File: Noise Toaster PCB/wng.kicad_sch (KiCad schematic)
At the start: 12 parts, among them Q2 2N3904, Q5 2N3904, Q6 2N3904

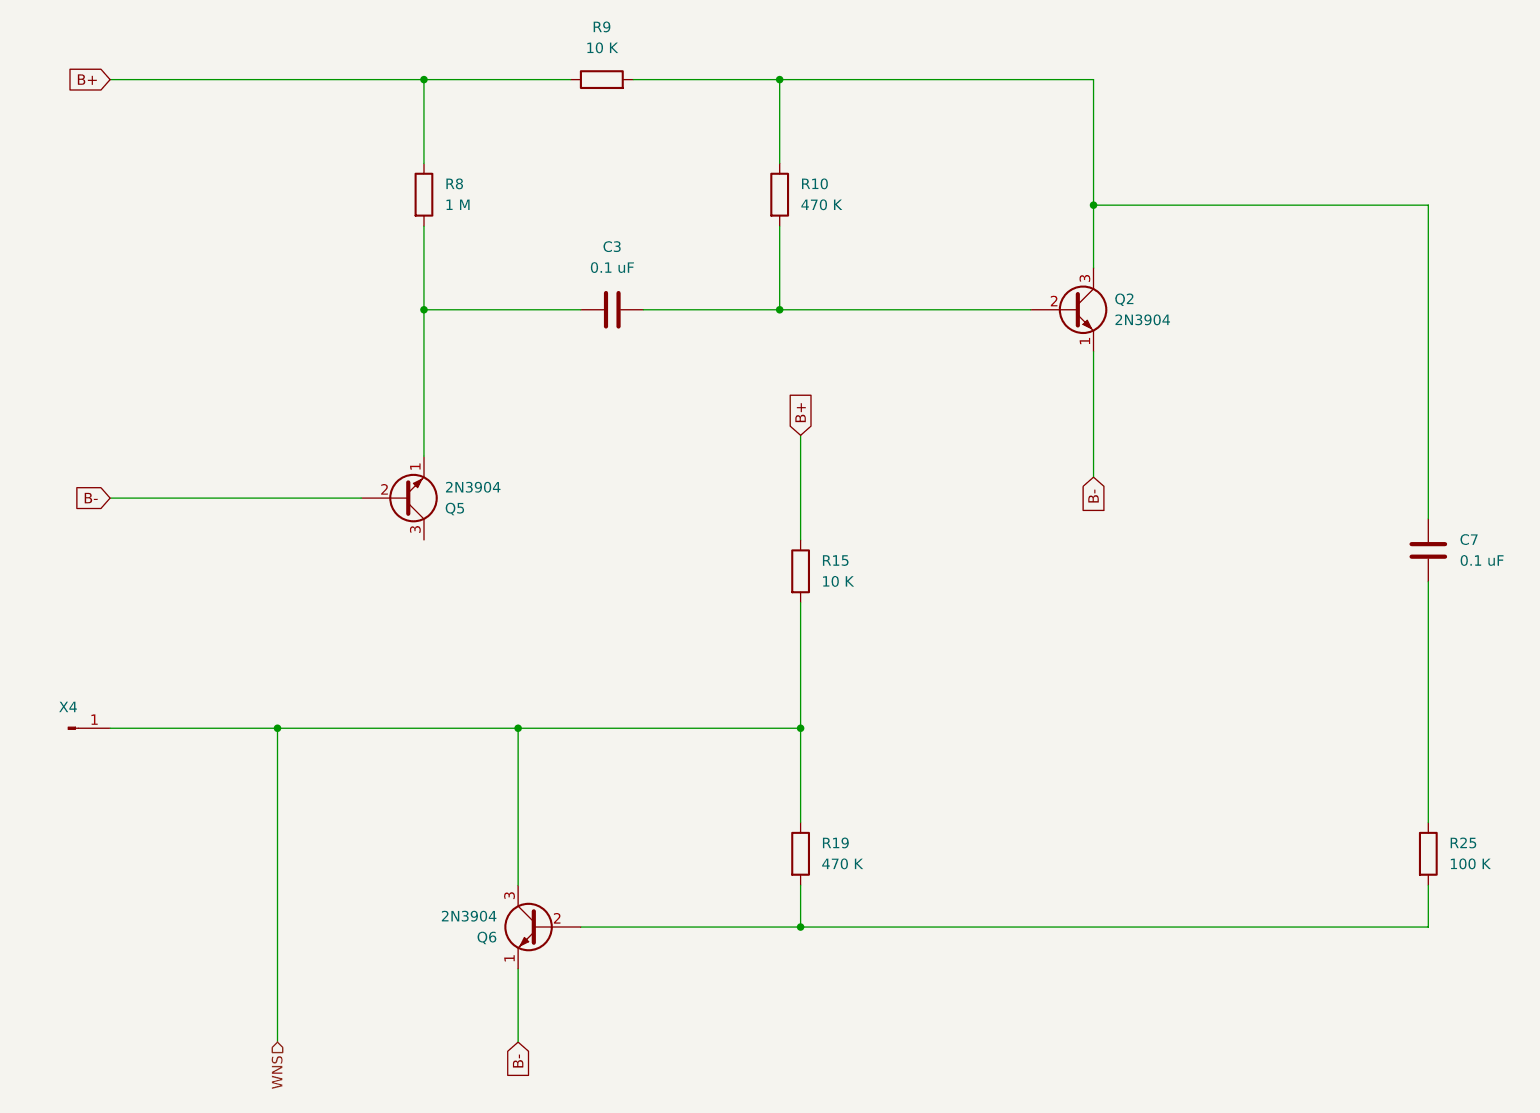
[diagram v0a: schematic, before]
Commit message: updated schematics
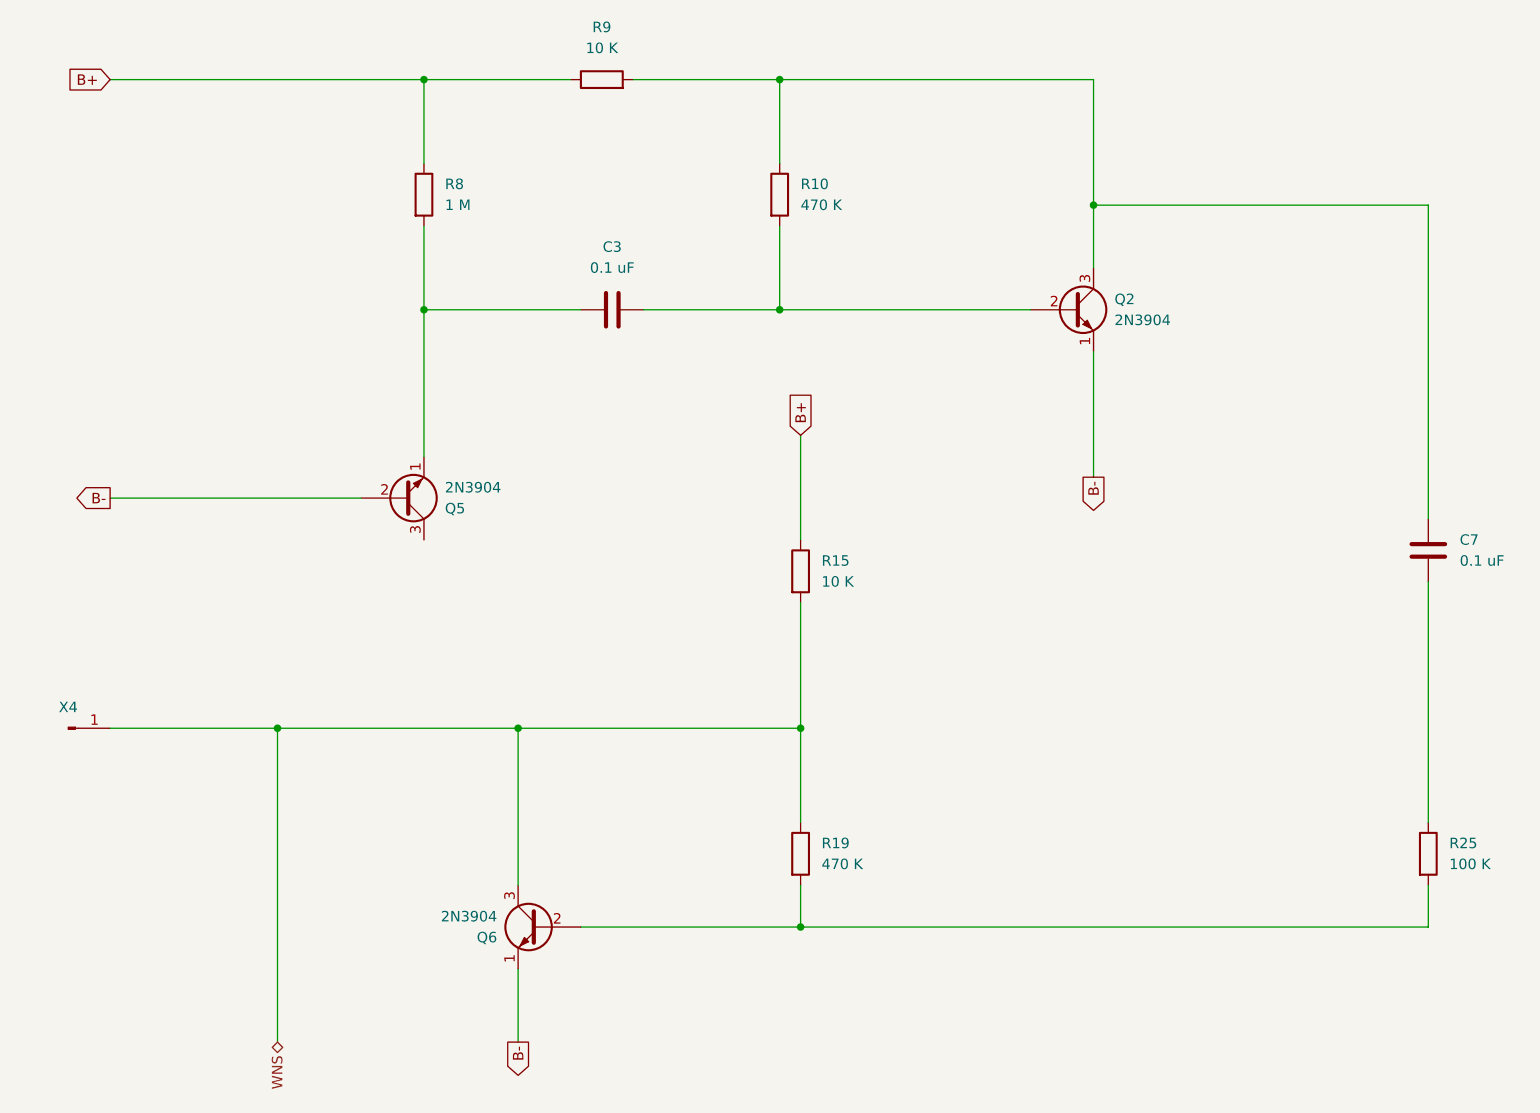
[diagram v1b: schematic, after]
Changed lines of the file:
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@@
     (stroke (width 0) (type default))
   )
-  (global_label "B-" (shape input) (at 118.11 165.1 270) (fields_autoplaced)
+  (global_label "B-" (shape output) (at 118.11 165.1 270) (fields_autoplaced)
     (effects (font (size 1.27 1.27)) (justify right))
     (property "Intersheetrefs" "${INTERSHEET_REFS}" (at 118.11 170.9276 90)
@@
     )
   )
-  (global_label "B-" (shape input) (at 187.96 96.52 270) (fields_autoplaced)
+  (global_label "B-" (shape output) (at 187.96 96.52 270) (fields_autoplaced)
     (effects (font (size 1.27 1.27)) (justify right))
     (property "Intersheetrefs" "${INTERSHEET_REFS}" (at 187.96 102.3476 90)
@@
     )
   )
-  (global_label "B-" (shape input) (at 68.58 99.06 180) (fields_autoplaced)
+  (global_label "B-" (shape output) (at 68.58 99.06 180) (fields_autoplaced)
     (effects (font (size 1.27 1.27)) (justify right))
     (property "Intersheetrefs" "${INTERSHEET_REFS}" (at 62.7524 99.06 0)
@@
     )
   )
-  (hierarchical_label "WNS" (shape input) (at 88.9 165.1 270) (fields_autoplaced)
+  (hierarchical_label "WNS" (shape bidirectional) (at 88.9 165.1 270) (fields_autoplaced)
     (effects (font (size 1.27 1.27)) (justify right))
   )

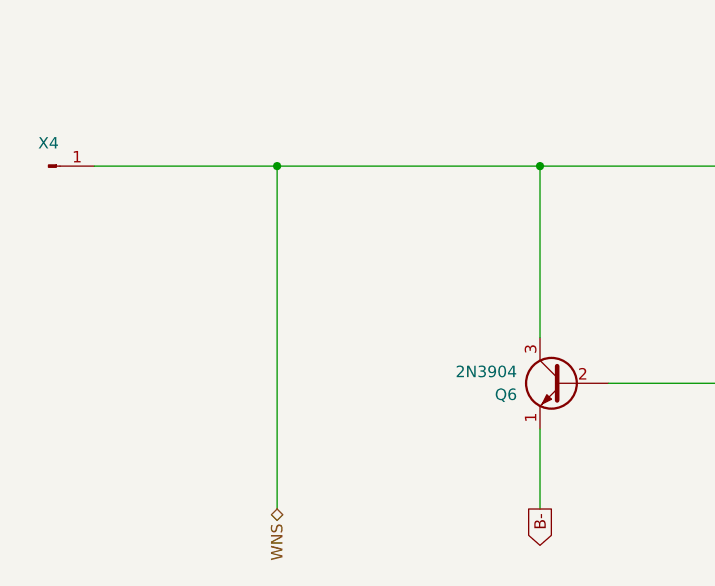
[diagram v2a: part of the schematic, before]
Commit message: refactored schematics and added front panel
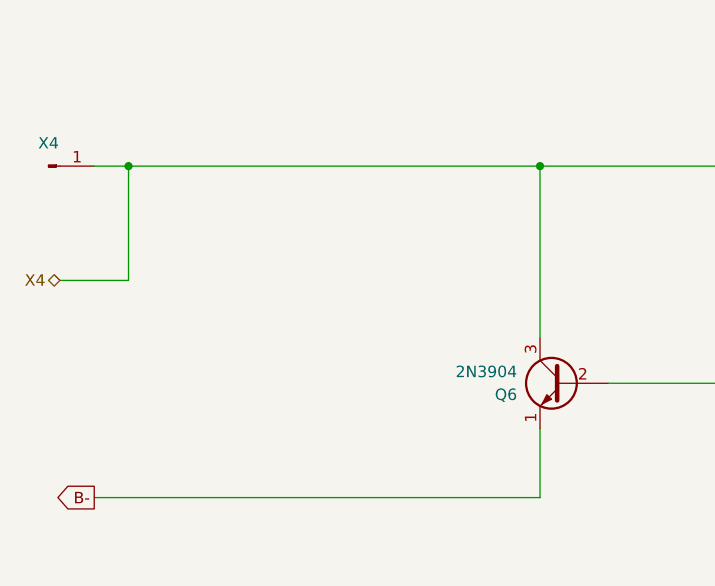
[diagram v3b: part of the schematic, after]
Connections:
- net WNS renamed X4
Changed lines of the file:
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@@
   (junction (at 106.68 48.26) (diameter 0) (color 0 0 0 0)
+  )
+  (junction (at 72.39 127) (diameter 0) (color 0 0 0 0)
   )
   (junction (at 187.96 63.5) (diameter 0) (color 0 0 0 0)
@@
   )
   (junction (at 149.86 76.2) (diameter 0) (color 0 0 0 0)
-  )
-  (junction (at 88.9 127) (diameter 0) (color 0 0 0 0)
   )
   (junction (at 106.68 76.2) (diameter 0) (color 0 0 0 0)
@@
     (stroke (width 0) (type default))
   )
-  (wire (pts (xy 118.11 156.21) (xy 118.11 165.1))
-    (stroke (width 0) (type default))
-  )
   (wire (pts (xy 149.86 76.2) (xy 180.34 76.2))
     (stroke (width 0) (type default))
   )
   (wire (pts (xy 106.68 76.2) (xy 125.73 76.2))
-    (stroke (width 0) (type default))
-  )
-  (wire (pts (xy 88.9 127) (xy 88.9 165.1))
     (stroke (width 0) (type default))
   )
@@
     (stroke (width 0) (type default))
   )
+  (wire (pts (xy 64.77 139.7) (xy 72.39 139.7))
+    (stroke (width 0) (type default))
+  )
   (wire (pts (xy 125.73 151.13) (xy 152.4 151.13))
     (stroke (width 0) (type default))
@@
     (stroke (width 0) (type default))
   )
+  (wire (pts (xy 118.11 163.83) (xy 118.11 156.21))
+    (stroke (width 0) (type default))
+  )
+  (wire (pts (xy 68.58 127) (xy 72.39 127))
+    (stroke (width 0) (type default))
+  )
+  (wire (pts (xy 72.39 127) (xy 118.11 127))
+    (stroke (width 0) (type default))
+  )
   (wire (pts (xy 152.4 91.44) (xy 152.4 104.14))
     (stroke (width 0) (type default))
   )
   (wire (pts (xy 133.35 76.2) (xy 149.86 76.2))
-    (stroke (width 0) (type default))
-  )
-  (wire (pts (xy 68.58 127) (xy 88.9 127))
     (stroke (width 0) (type default))
   )
@@
     (stroke (width 0) (type default))
   )
+  (wire (pts (xy 68.58 163.83) (xy 118.11 163.83))
+    (stroke (width 0) (type default))
+  )
   (wire (pts (xy 187.96 63.5) (xy 187.96 48.26))
     (stroke (width 0) (type default))
   )
-  (wire (pts (xy 187.96 81.28) (xy 187.96 96.52))
+  (wire (pts (xy 72.39 139.7) (xy 72.39 127))
     (stroke (width 0) (type default))
   )
-  (wire (pts (xy 88.9 127) (xy 118.11 127))
+  (wire (pts (xy 187.96 81.28) (xy 187.96 96.52))
     (stroke (width 0) (type default))
   )
@@
     (stroke (width 0) (type default))
   )
-  (global_label "B-" (shape output) (at 118.11 165.1 270) (fields_autoplaced)
+  (global_label "B-" (shape output) (at 68.58 163.83 180) (fields_autoplaced)
     (effects (font (size 1.27 1.27)) (justify right))
-    (property "Intersheetrefs" "${INTERSHEET_REFS}" (at 118.11 170.9276 90)
+    (property "Intersheetrefs" "${INTERSHEET_REFS}" (at 62.7524 163.83 0)
       (effects (font (size 1.27 1.27)) (justify right) hide)
     )
@@
     )
   )
-  (hierarchical_label "WNS" (shape bidirectional) (at 88.9 165.1 270)
+  (hierarchical_label "X4" (shape bidirectional) (at 64.77 139.7 180)
     (effects (font (size 1.27 1.27)) (justify right))
-    (property "Bezeichnung" "X4" (at 86.36 165.1 0)
-      (effects (font (size 1.27 1.27) italic) (justify right))
+    (property "Bezeichnung" "WNS" (at 60.96 137.16 0)
+      (effects (font (size 1.27 1.27) italic) (justify left))
     )
   )

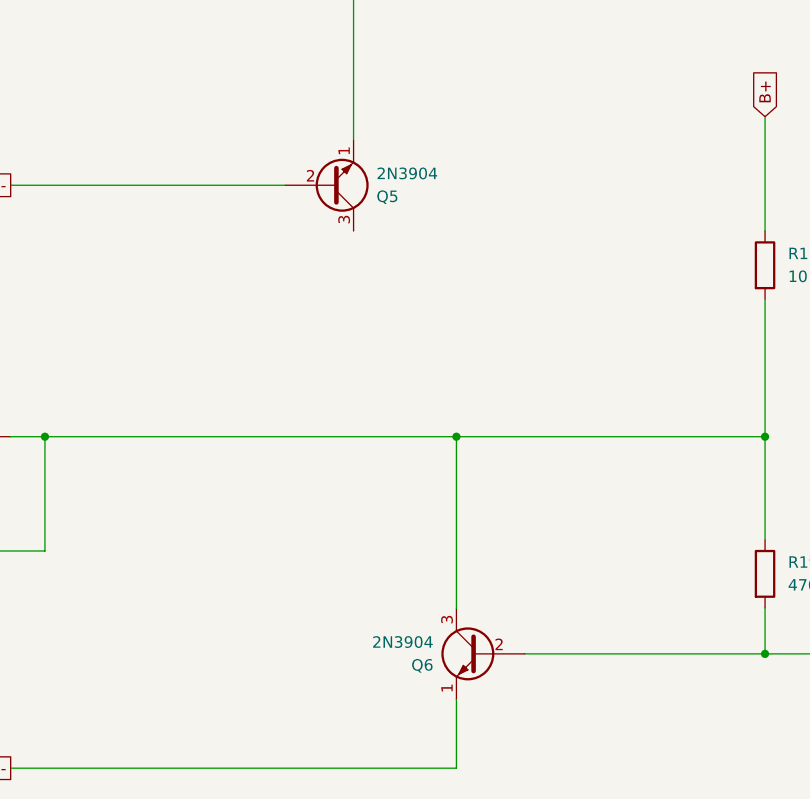
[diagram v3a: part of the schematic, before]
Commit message: wireing and components have been checked
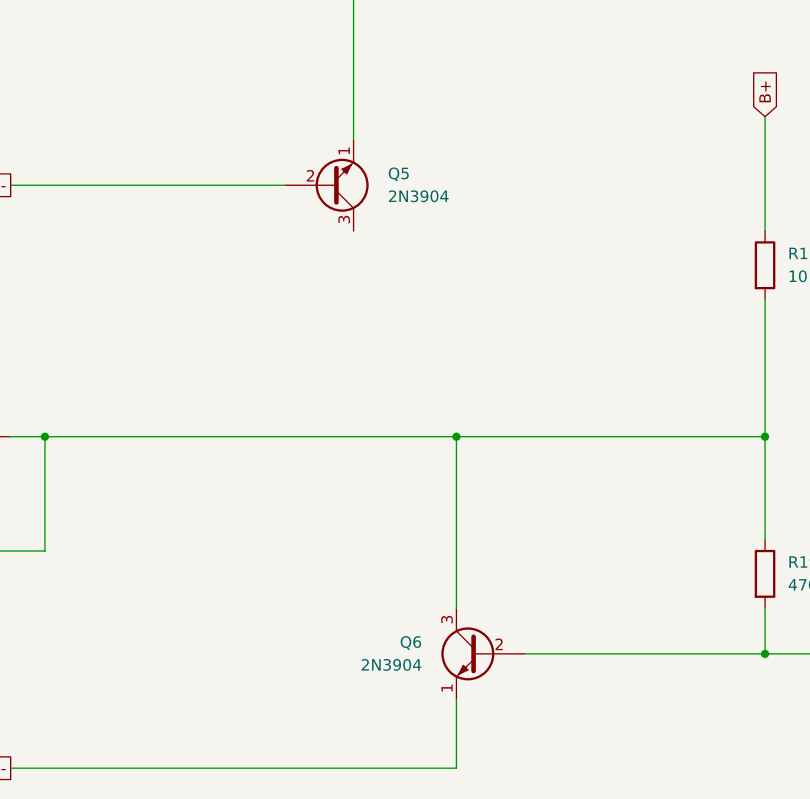
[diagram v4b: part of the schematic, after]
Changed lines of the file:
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@@
   (symbol (lib_id "Transistor_BJT:2N3904") (at 104.14 99.06 0) (mirror x) (unit 1)
     (in_bom yes) (on_board yes) (dnp no)
-    (property "Reference" "Q5" (at 109.22 100.33 0)
+    (property "Reference" "Q5" (at 110.49 97.79 0)
       (effects (font (size 1.27 1.27)) (justify left))
     )
-    (property "Value" "2N3904" (at 109.22 97.79 0)
+    (property "Value" "2N3904" (at 110.49 100.33 0)
       (effects (font (size 1.27 1.27)) (justify left))
     )
@@
   (symbol (lib_id "Transistor_BJT:2N3904") (at 120.65 151.13 0) (mirror y) (unit 1)
     (in_bom yes) (on_board yes) (dnp no)
-    (property "Reference" "Q6" (at 115.57 152.4 0)
+    (property "Reference" "Q6" (at 114.3 149.86 0)
       (effects (font (size 1.27 1.27)) (justify left))
     )
-    (property "Value" "2N3904" (at 115.57 149.86 0)
+    (property "Value" "2N3904" (at 114.3 152.4 0)
       (effects (font (size 1.27 1.27)) (justify left))
     )

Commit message: applied footprints
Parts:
- C3, C7: footprint (none) -> Capacitor_THT:C_Disc_D5.1mm_W3.2mm_P5.00mm
- R10, R15, R19, R25, R8, R9: footprint (none) -> Resistor_THT:R_Axial_DIN0207_L6.3mm_D2.5mm_P10.16mm_Horizontal
- X4: footprint (none) -> Connector_PinHeader_1.00mm:PinHeader_1x01_P1.00mm_Vertical
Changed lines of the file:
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@@
       (effects (font (size 1.27 1.27)) (justify left))
     )
-    (property "Footprint" "" (at 104.902 62.23 90)
+    (property "Footprint" "Resistor_THT:R_Axial_DIN0207_L6.3mm_D2.5mm_P10.16mm_Horizontal" (at 104.902 62.23 90)
       (effects (font (size 1.27 1.27)) hide)
     )
@@
       (effects (font (size 1.27 1.27)))
     )
-    (property "Footprint" "" (at 63.5 127 0)
+    (property "Footprint" "Connector_PinHeader_1.00mm:PinHeader_1x01_P1.00mm_Vertical" (at 63.5 127 0)
       (effects (font (size 1.27 1.27)) hide)
     )
@@
       (effects (font (size 1.27 1.27)))
     )
-    (property "Footprint" "" (at 128.27 50.038 90)
+    (property "Footprint" "Resistor_THT:R_Axial_DIN0207_L6.3mm_D2.5mm_P10.16mm_Horizontal" (at 128.27 50.038 90)
       (effects (font (size 1.27 1.27)) hide)
     )
@@
       (effects (font (size 1.27 1.27)))
     )
-    (property "Footprint" "" (at 133.35 75.2348 0)
+    (property "Footprint" "Capacitor_THT:C_Disc_D5.1mm_W3.2mm_P5.00mm" (at 133.35 75.2348 0)
       (effects (font (size 1.27 1.27)) hide)
     )
@@
       (effects (font (size 1.27 1.27)) (justify left))
     )
-    (property "Footprint" "" (at 150.622 142.24 90)
+    (property "Footprint" "Resistor_THT:R_Axial_DIN0207_L6.3mm_D2.5mm_P10.16mm_Horizontal" (at 150.622 142.24 90)
       (effects (font (size 1.27 1.27)) hide)
     )
@@
       (effects (font (size 1.27 1.27)) (justify left))
     )
-    (property "Footprint" "" (at 148.082 62.23 90)
+    (property "Footprint" "Resistor_THT:R_Axial_DIN0207_L6.3mm_D2.5mm_P10.16mm_Horizontal" (at 148.082 62.23 90)
       (effects (font (size 1.27 1.27)) hide)
     )
@@
       (effects (font (size 1.27 1.27)) (justify left))
     )
-    (property "Footprint" "" (at 226.822 142.24 90)
+    (property "Footprint" "Resistor_THT:R_Axial_DIN0207_L6.3mm_D2.5mm_P10.16mm_Horizontal" (at 226.822 142.24 90)
       (effects (font (size 1.27 1.27)) hide)
     )
@@
       (effects (font (size 1.27 1.27)) (justify left))
     )
-    (property "Footprint" "" (at 229.5652 109.22 0)
+    (property "Footprint" "Capacitor_THT:C_Disc_D5.1mm_W3.2mm_P5.00mm" (at 229.5652 109.22 0)
       (effects (font (size 1.27 1.27)) hide)
     )
@@
       (effects (font (size 1.27 1.27)) (justify left))
     )
-    (property "Footprint" "" (at 150.622 107.95 90)
-      (effects (font (size 1.27 1.27)) hide)
-    )
+    (property "Footprint" "Resistor_THT:R_Axial_DIN0207_L6.3mm_D2.5mm_P10.16mm_Horizontal" (at 150.622 107.95 90)
+      (effects (font (size 1.27 1.27)) hide)
+    )

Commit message: placed pards of the pcb properly
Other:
- company: http://musicfromouterspace.com/analogsynth_new/NOISETOASTER/NOISETOASTER.php -> Music From Outer Space LLC
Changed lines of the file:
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@@
     (title "White Noise Generator")
     (rev "0.5")
-    (company "http://musicfromouterspace.com/analogsynth_new/NOISETOASTER/NOISETOASTER.php")
+    (company "Music From Outer Space LLC")
     (comment 1 "Licence: CC-BY-NC-SA")
     (comment 2 "Original Design by Ray Wilson")
-    (comment 3 "Music From Outer Space LLC")
+    (comment 3 "http://musicfromouterspace.com/analogsynth_new/NOISETOASTER/NOISETOASTER.php")
   )
   (junction (at 149.86 48.26) (diameter 0) (color 0 0 0 0)

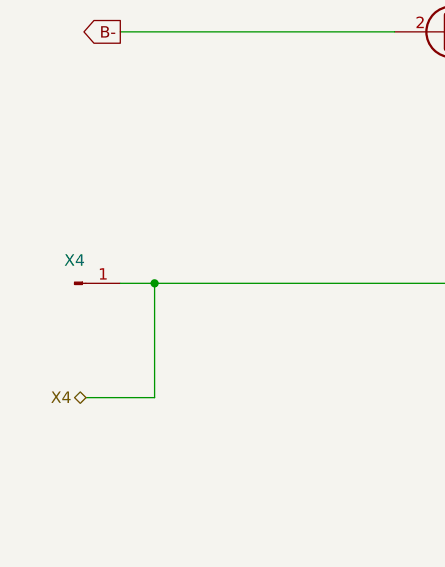
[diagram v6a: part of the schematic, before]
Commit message: changed header pins to groups
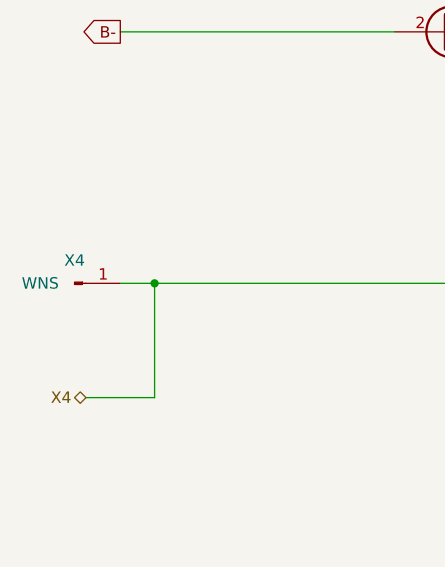
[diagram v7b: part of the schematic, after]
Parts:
- X4: value ~ -> WNS; footprint Connector_PinHeader_1.00mm:PinHeader_1x01_P1.00mm_Vertical -> Connector_PinHeader_2.00mm:PinHeader_1x01_P2.00mm_Vertical
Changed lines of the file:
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@@
   (title_block
     (title "White Noise Generator")
-    (rev "0.5")
+    (rev "0.6")
     (company "Music From Outer Space LLC")
     (comment 1 "Licence: CC-BY-NC-SA")
@@
       (effects (font (size 1.27 1.27)))
     )
-    (property "Value" "~" (at 64.135 124.46 0)
+    (property "Value" "WNS" (at 59.69 127 0)
       (effects (font (size 1.27 1.27)))
     )
-    (property "Footprint" "Connector_PinHeader_1.00mm:PinHeader_1x01_P1.00mm_Vertical" (at 63.5 127 0)
+    (property "Footprint" "Connector_PinHeader_2.00mm:PinHeader_1x01_P2.00mm_Vertical" (at 63.5 127 0)
       (effects (font (size 1.27 1.27)) hide)
     )
